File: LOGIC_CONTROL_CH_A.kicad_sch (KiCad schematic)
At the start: 47 parts, among them IC53 ${DEVICE}, IC54 ${DEVICE}, IC55 ${DEVICE}, IC56 ${DEVICE}, IC57 ${DEVICE}, IC58 ${DEVICE}, IC59 ${DEVICE}

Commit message: Updated schematic and rerouted PCB
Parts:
- removed C159, C160, C161, C162, C163, C164, C165, C166: 100nF, Capacitors SMD:CAPC1005X55N, symbol CERN:Capacitors SMD/CC0402_100NF_25V_10%_X7R_YUDEN_TMK105B7104KVHF
- added C10, C11, C12, C13, C14, C15, C8, C9: 100nF, Capacitors SMD:CAPC1608X87N, symbol CERN:Capacitors SMD/CC0603_100NF_50V_10%_X7R
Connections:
- net GND: now also C10.1, C11.1, C12.1, C13.1, C14.1, C15.1, C8.1, C9.1
- net VCCA: now also C11.2
- net at IC54.16 (VCC), L27.1: now also C12.2
- net at IC57.20 (VCC), L30.1: now also C13.2
- net at IC59.19 (VCCB), L32.1: now also C10.2
- net at IC58.20 (VCC), L31.1: now also C9.2
- net at IC55.16 (VCC), L28.1: now also C8.2
- net at IC53.16 (VCC), L26.1: now also C14.2
- net at IC56.20 (VCC), L29.1: now also C15.2

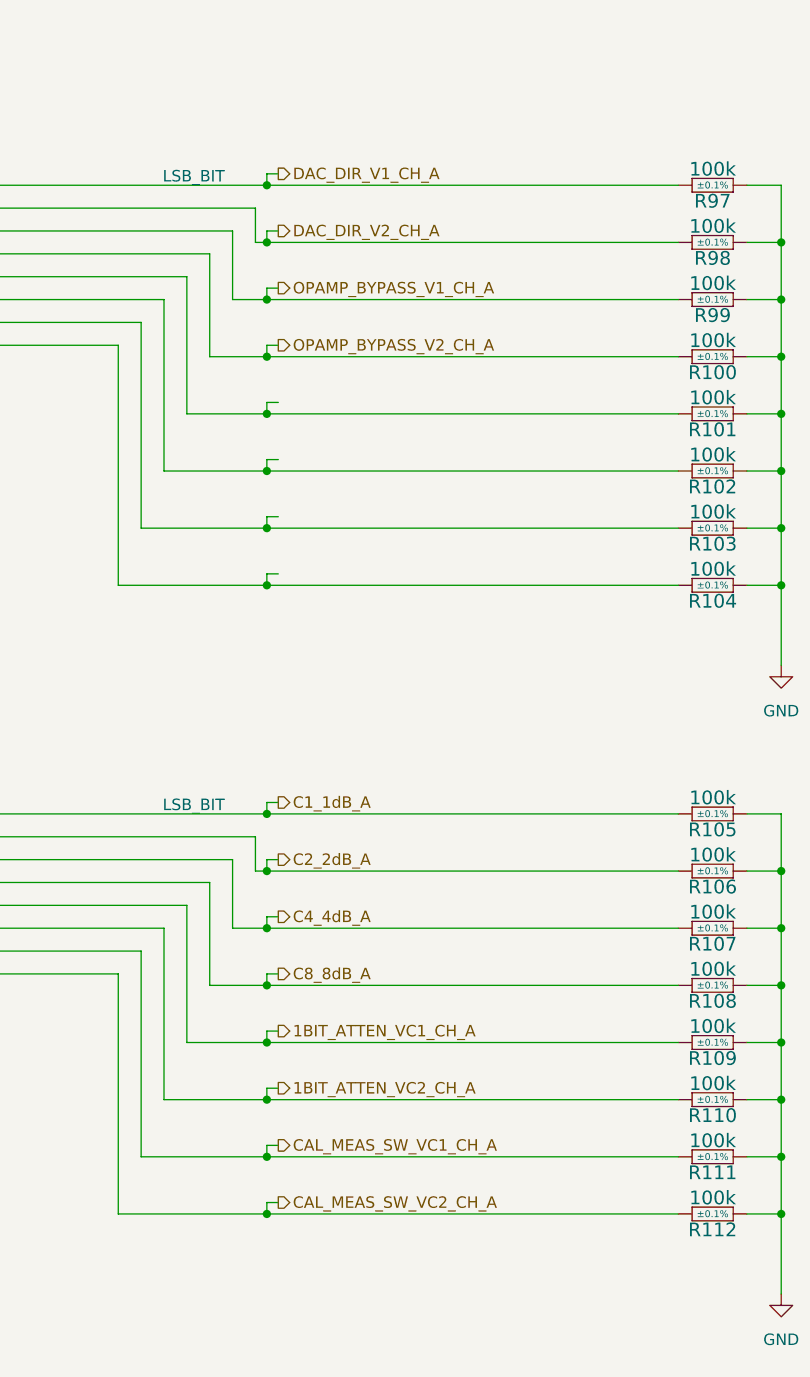
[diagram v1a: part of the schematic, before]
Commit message: Rerouted PCB Logic part
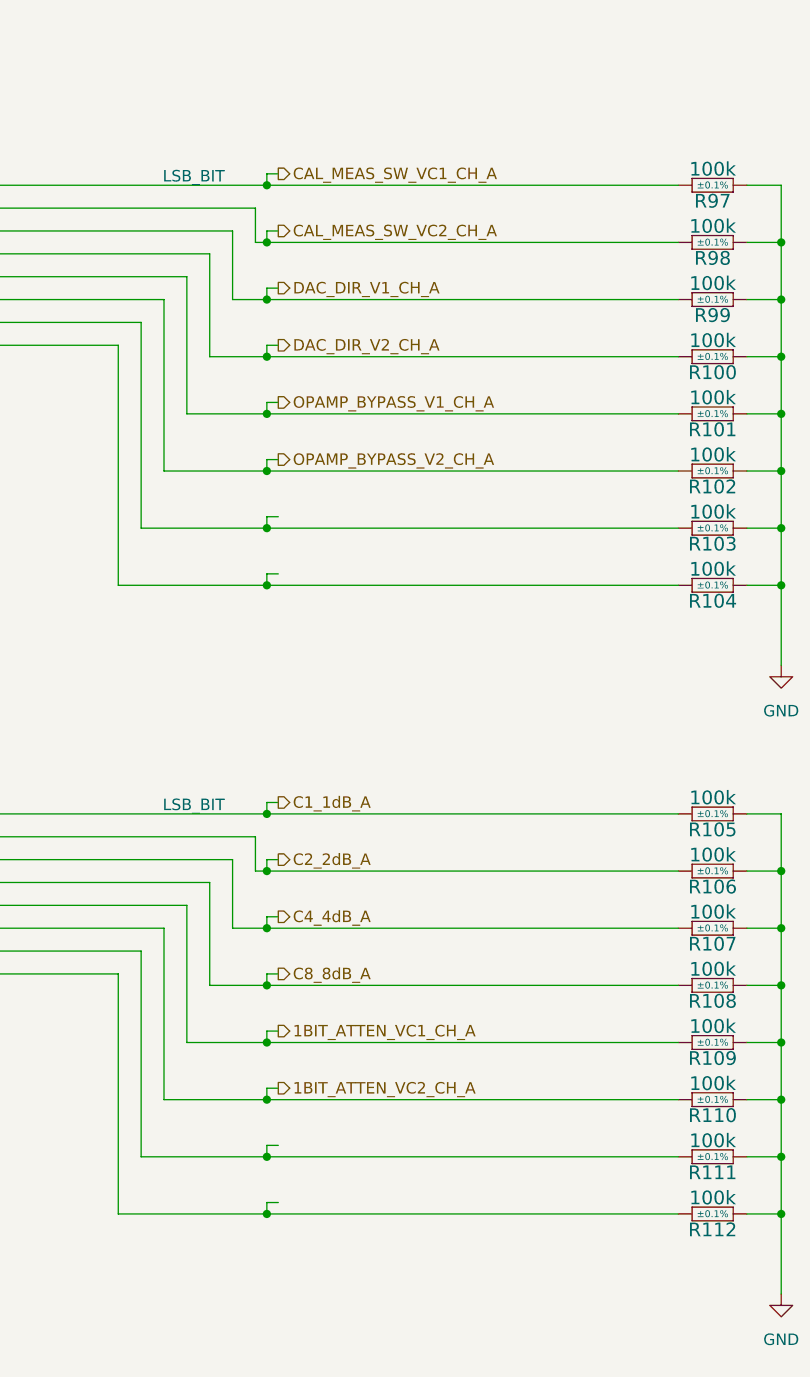
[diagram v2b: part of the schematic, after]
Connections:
- net CAL_MEAS_SW_VC1_CH_A: now also IC56.12 (Q8), R97.2; no longer IC57.18 (Q2), R111.2
- net CAL_MEAS_SW_VC2_CH_A: now also IC56.13 (Q7), R98.2; no longer IC57.19 (Q1), R112.2
- net DAC_DIR_V1_CH_A: now also IC56.14 (Q6), R99.2; no longer IC56.12 (Q8), R97.2
- net DAC_DIR_V2_CH_A: now also IC56.15 (Q5), R100.2; no longer IC56.13 (Q7), R98.2
- net OPAMP_BYPASS_V1_CH_A: now also IC56.16 (Q4), R101.2; no longer IC56.14 (Q6), R99.2
- net OPAMP_BYPASS_V2_CH_A: now also IC56.17 (Q3), R102.2; no longer IC56.15 (Q5), R100.2
- new net: IC57.18 (Q2), R111.2
- new net: IC57.19 (Q1), R112.2
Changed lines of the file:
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@@
-		)
-	)
-	(hierarchical_label "OPAMP_BYPASS_V2_CH_A"
-		(shape output)
-		(at 345.44 64.77 0)
-		(effects
-			(font
-				(size 1.27 1.27)
-			)
-			(justify left)
 		)
 	)
@@
 		(shape output)
 		(at 345.44 147.32 0)
-		(effects
-			(font
-				(size 1.27 1.27)
-			)
-			(justify left)
-		)
-	)
-	(hierarchical_label "DAC_DIR_V1_CH_A"
-		(shape output)
-		(at 345.44 45.72 0)
 		(effects
 			(font
@@
 		)
 	)
+	(hierarchical_label "DAC_DIR_V1_CH_A"
+		(shape output)
+		(at 345.44 58.42 0)
+		(effects
+			(font
+				(size 1.27 1.27)
+			)
+			(justify left)
+		)
+	)
 	(hierarchical_label "A0"
 		(shape output)
@@
 		)
 	)
+	(hierarchical_label "DAC_DIR_V2_CH_A"
+		(shape output)
+		(at 345.44 64.77 0)
+		(effects
+			(font
+				(size 1.27 1.27)
+			)
+			(justify left)
+		)
+	)
 	(hierarchical_label "A1"
 		(shape output)
@@
 		)
 	)
+	(hierarchical_label "C2_2dB_A"
+		(shape output)
+		(at 345.44 121.92 0)
+		(effects
+			(font
+				(size 1.27 1.27)
+			)
+			(justify left)
+		)
+	)
+	(hierarchical_label "A2"
+		(shape output)
+		(at 345.44 200.66 0)
+		(effects
+			(font
+				(size 1.27 1.27)
+			)
+			(justify left)
+		)
+	)
+	(hierarchical_label "C1_1dB_A"
+		(shape output)
+		(at 345.44 115.57 0)
+		(effects
+			(font
+				(size 1.27 1.27)
+			)
+			(justify left)
+		)
+	)
+	(hierarchical_label "CAL_MEAS_SW_VC2_CH_A"
+		(shape output)
+		(at 345.44 52.07 0)
+		(effects
+			(font
+				(size 1.27 1.27)
+			)
+			(justify left)
+		)
+	)
+	(hierarchical_label "A4"
+		(shape output)
+		(at 345.44 213.36 0)
+		(effects
+			(font
+				(size 1.27 1.27)
+			)
+			(justify left)
+		)
+	)
 	(hierarchical_label "OPAMP_BYPASS_V1_CH_A"
 		(shape output)
-		(at 345.44 58.42 0)
-		(effects
-			(font
-				(size 1.27 1.27)
-			)
-			(justify left)
-		)
-	)
-	(hierarchical_label "C2_2dB_A"
-		(shape output)
-		(at 345.44 121.92 0)
-		(effects
-			(font
-				(size 1.27 1.27)
-			)
-			(justify left)
-		)
-	)
-	(hierarchical_label "CAL_MEAS_SW_VC2_CH_A"
-		(shape output)
-		(at 345.44 160.02 0)
-		(effects
-			(font
-				(size 1.27 1.27)
-			)
-			(justify left)
-		)
-	)
-	(hierarchical_label "A2"
-		(shape output)
-		(at 345.44 200.66 0)
-		(effects
-			(font
-				(size 1.27 1.27)
-			)
-			(justify left)
-		)
-	)
-	(hierarchical_label "C1_1dB_A"
-		(shape output)
-		(at 345.44 115.57 0)
-		(effects
-			(font
-				(size 1.27 1.27)
-			)
-			(justify left)
-		)
-	)
-	(hierarchical_label "A4"
-		(shape output)
-		(at 345.44 213.36 0)
+		(at 345.44 71.12 0)
+		(effects
+			(font
+				(size 1.27 1.27)
+			)
+			(justify left)
+		)
+	)
+	(hierarchical_label "OPAMP_BYPASS_V2_CH_A"
+		(shape output)
+		(at 345.44 77.47 0)
 		(effects
 			(font
@@
 		(shape output)
 		(at 345.44 128.27 0)
-		(effects
-			(font
-				(size 1.27 1.27)
-			)
-			(justify left)
-		)
-	)
-	(hierarchical_label "CAL_MEAS_SW_VC1_CH_A"
-		(shape output)
-		(at 345.44 153.67 0)
 		(effects
 			(font
@@
 		)
 	)
-	(hierarchical_label "DAC_DIR_V2_CH_A"
-		(shape output)
-		(at 345.44 52.07 0)
-		(effects
-			(font
+	(hierarchical_label "CAL_MEAS_SW_VC1_CH_A"
+		(shape output)
+		(at 345.44 45.72 0)
+		(effects
+			(font

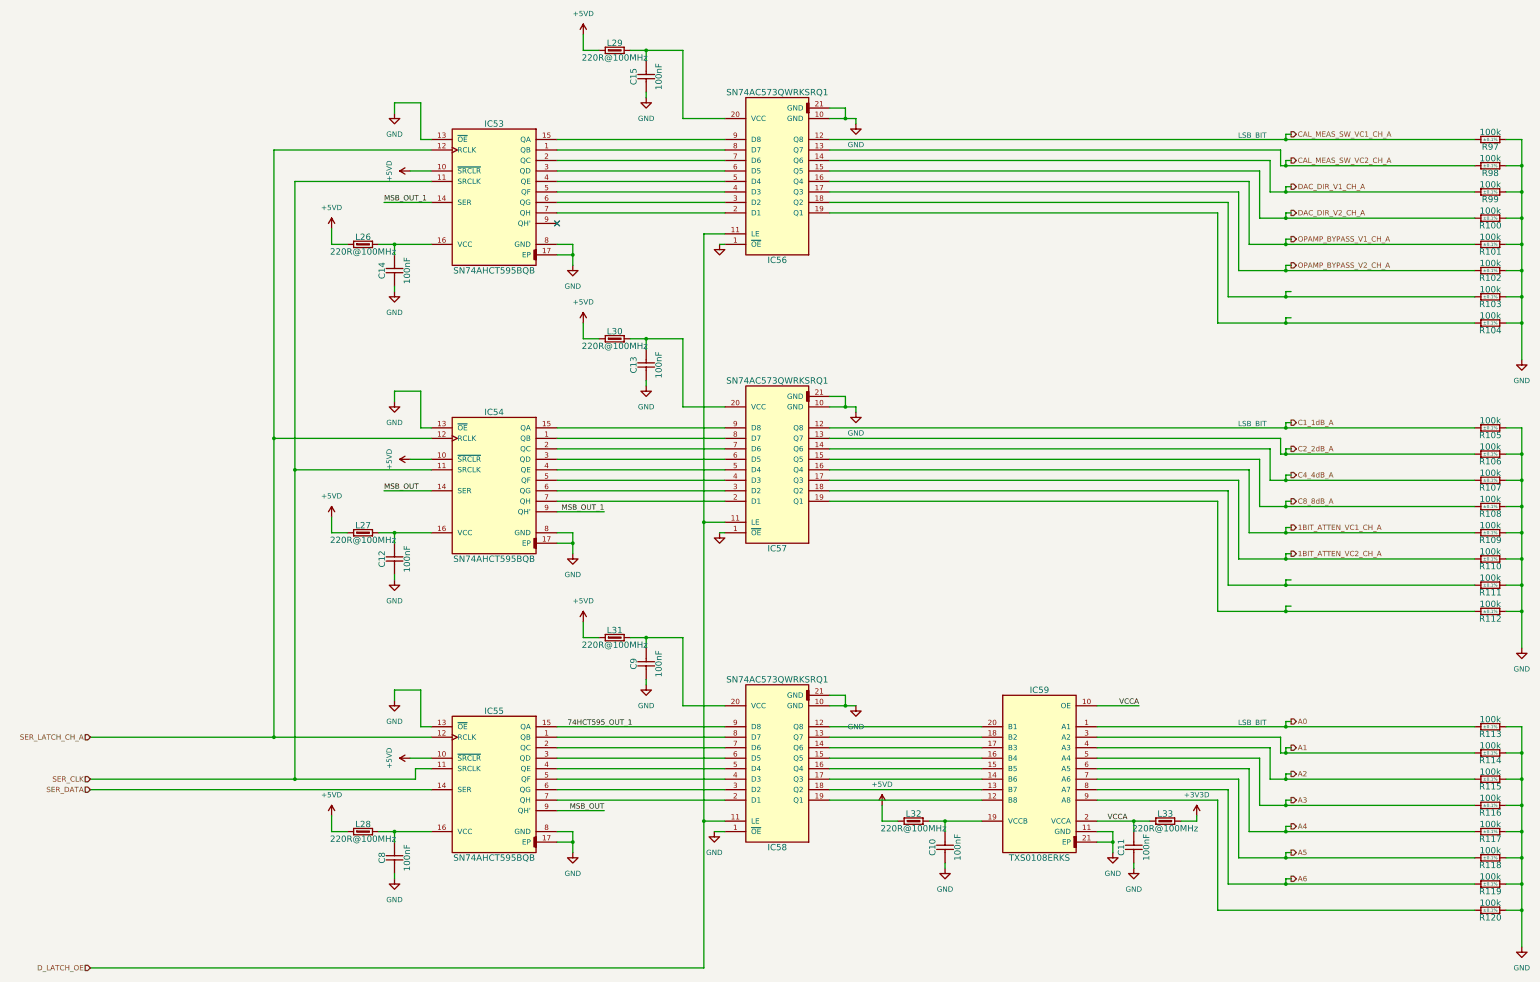
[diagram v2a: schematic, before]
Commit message: Rerouted PCB Logic part
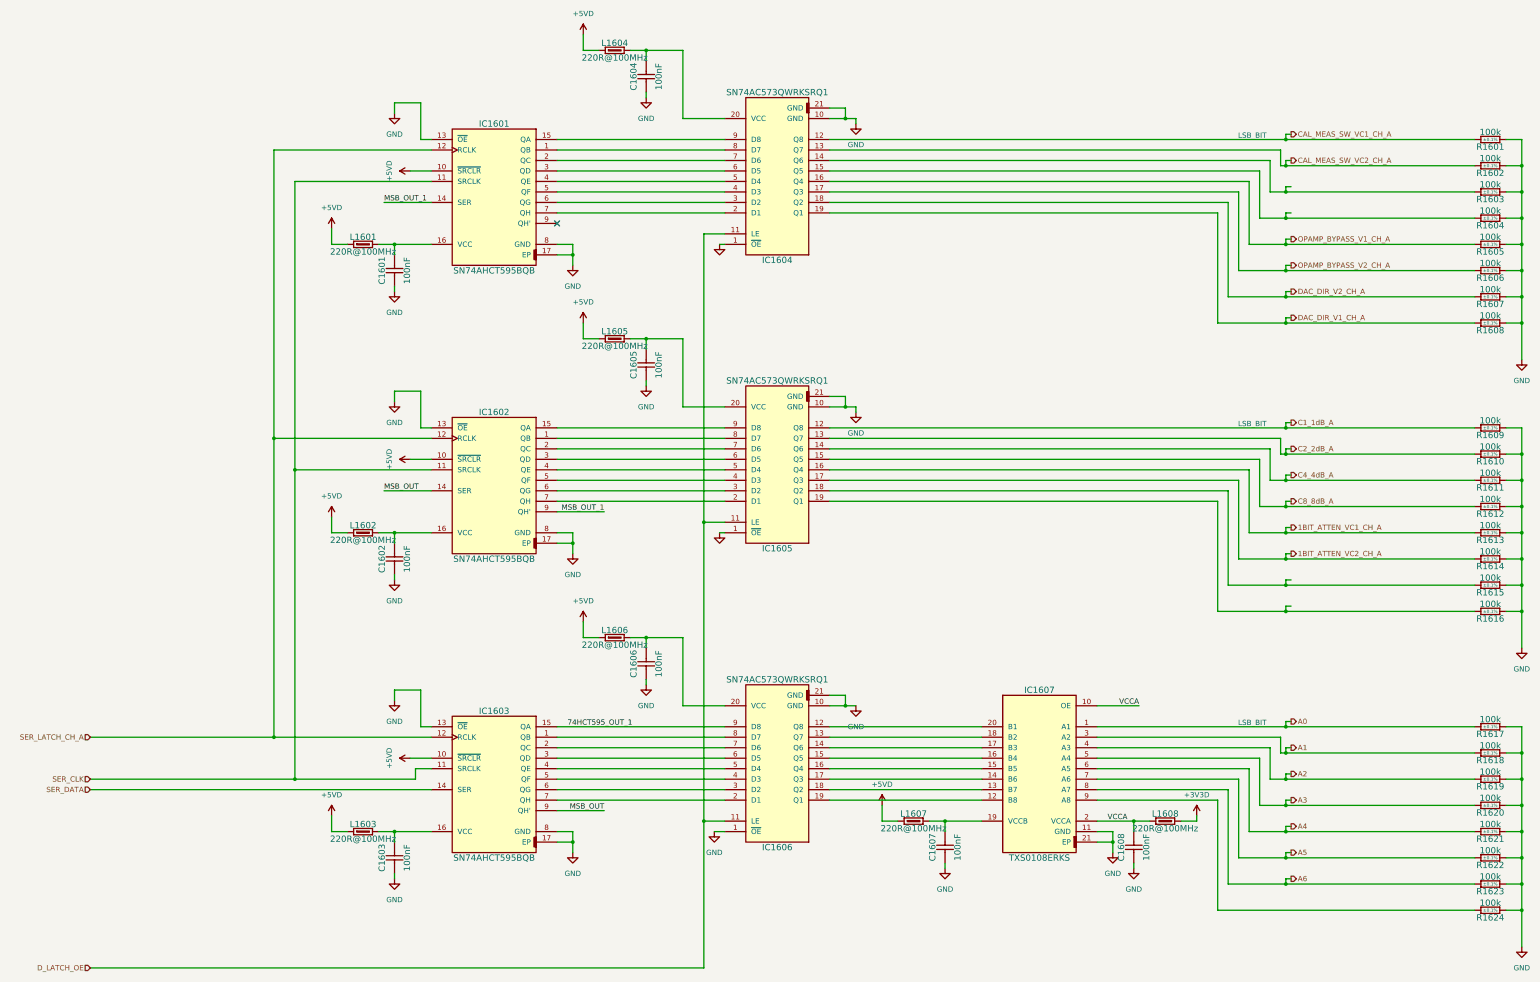
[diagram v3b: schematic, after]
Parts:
- renumbered C14 to C1601, C12 to C1602, C8 to C1603, C15 to C1604, C13 to C1605, C9 to C1606, C10 to C1607, C11 to C1608, IC53 to IC1601, IC54 to IC1602, IC55 to IC1603, IC56 to IC1604, IC57 to IC1605, IC58 to IC1606, IC59 to IC1607, L26 to L1601, L27 to L1602, L28 to L1603, L29 to L1604, L30 to L1605, L31 to L1606, L32 to L1607, L33 to L1608, R97 to R1601, R98 to R1602, R99 to R1603, R100 to R1604, R101 to R1605, R102 to R1606, R103 to R1607, R104 to R1608, R105 to R1609, R106 to R1610, R107 to R1611, R108 to R1612, R109 to R1613, R110 to R1614, R111 to R1615, R112 to R1616, R113 to R1617, R114 to R1618, R115 to R1619, R116 to R1620, R117 to R1621, R118 to R1622, R119 to R1623, R120 to R1624
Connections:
- net DAC_DIR_V1_CH_A: now also IC1604.19 (Q1), R1608.2; no longer IC1604.14 (Q6), R1603.2
- net DAC_DIR_V2_CH_A: now also IC1604.18 (Q2), R1607.2; no longer IC1604.15 (Q5), R1604.2
- new net: IC1604.14 (Q6), R1603.2
- new net: IC1604.15 (Q5), R1604.2
